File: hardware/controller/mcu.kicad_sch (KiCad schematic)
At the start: 13 parts, among them J5 Screw_Terminal_01x02, J6 Screw_Terminal_01x02, P1 USB_C_Plug_USB2.0, Q1 MMBF4392, U1 ESP32-C3-MINI-1

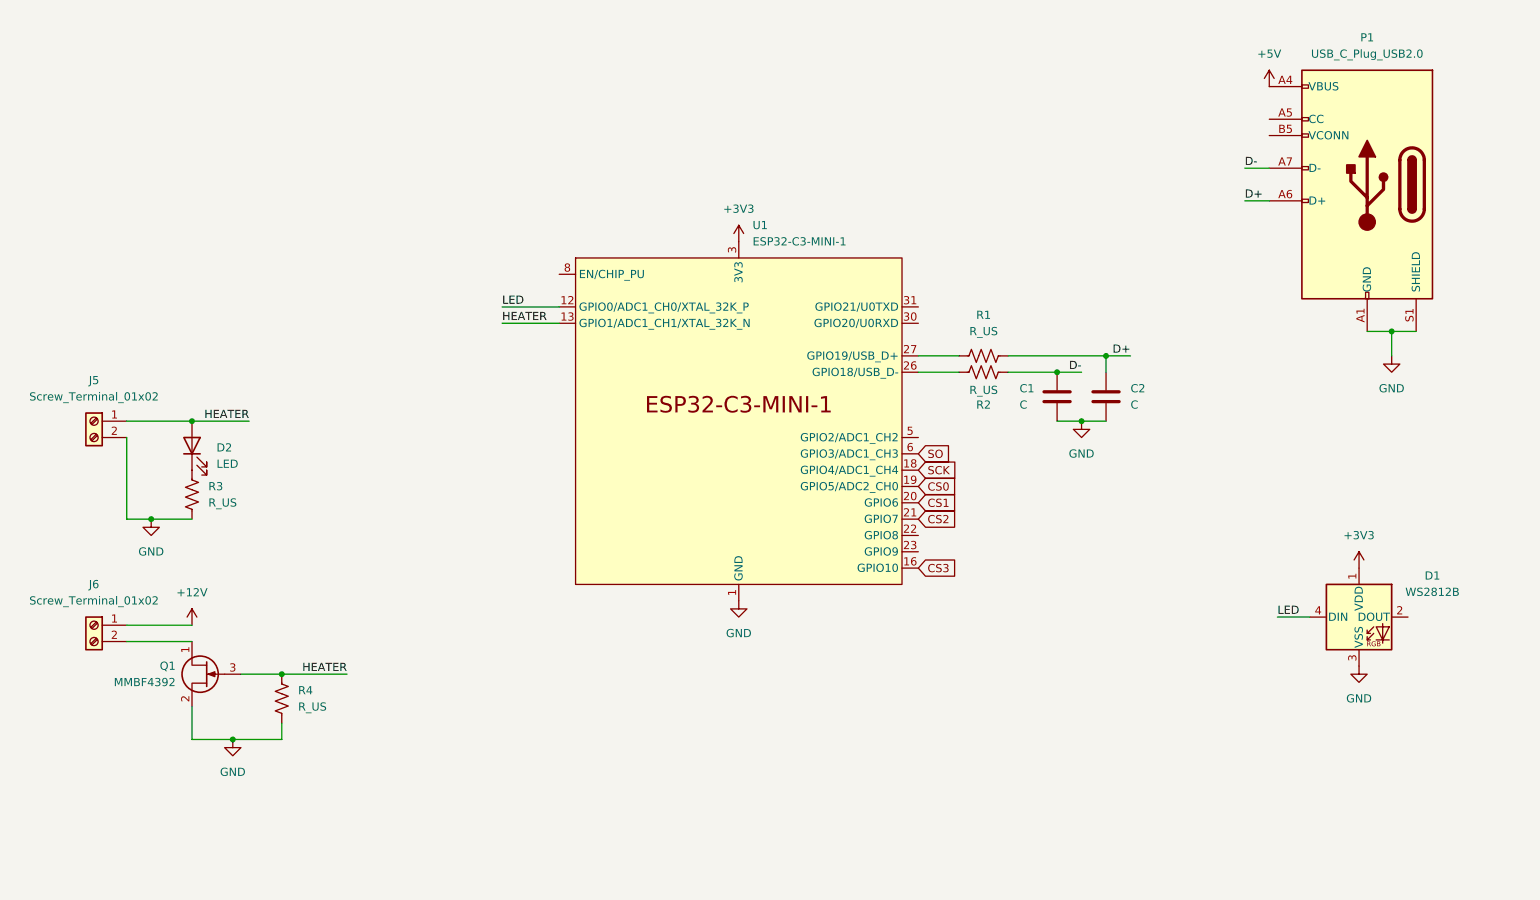
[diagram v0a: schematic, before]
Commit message: Fixed up MCU strapping pins
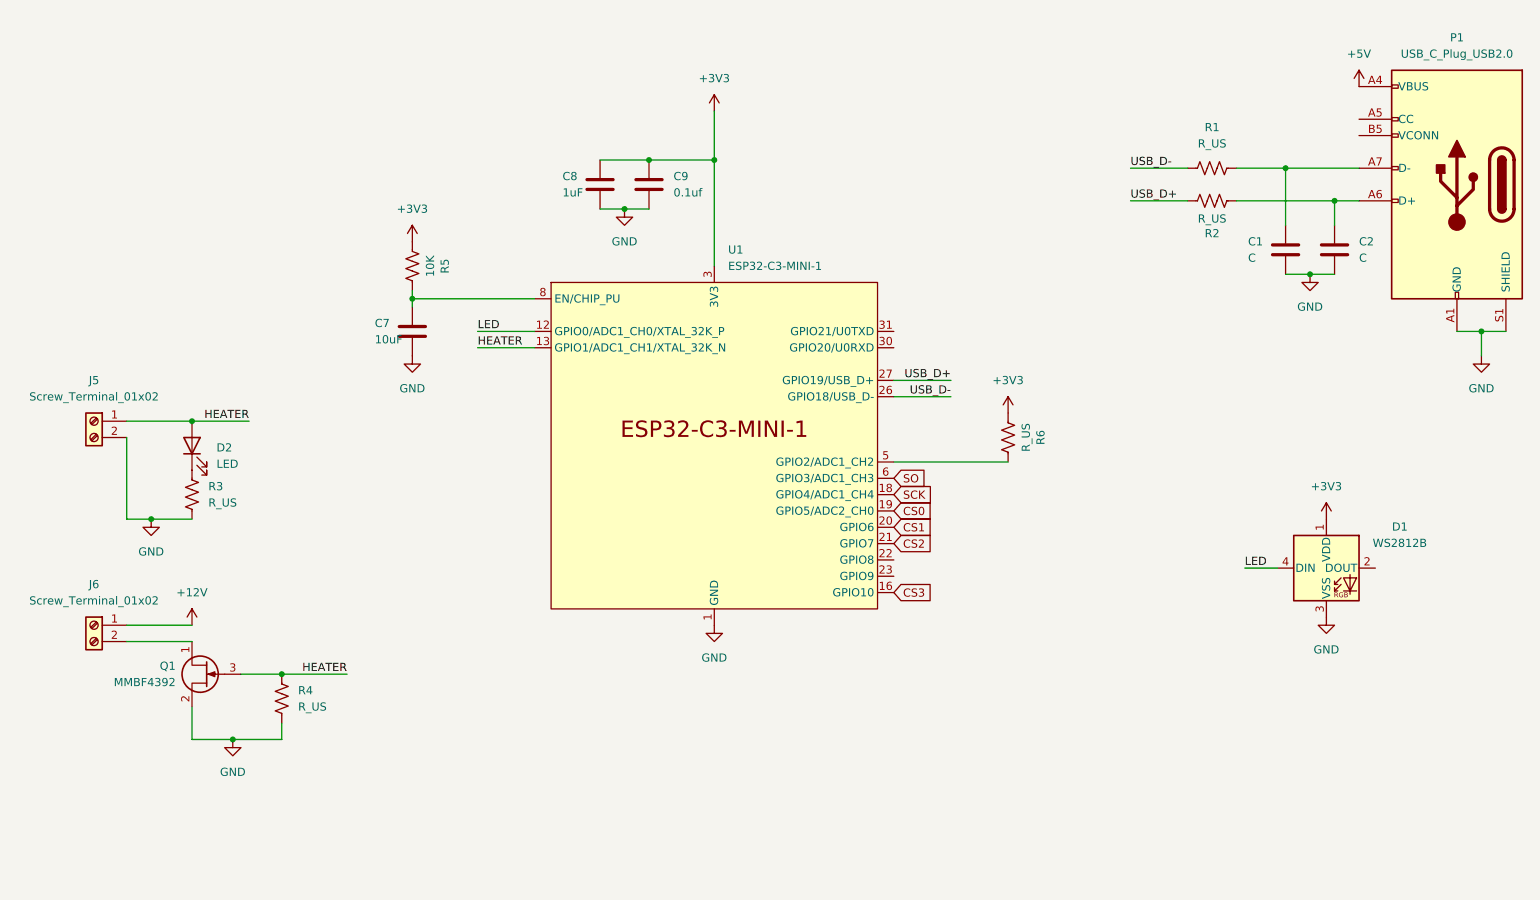
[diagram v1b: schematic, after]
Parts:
- added C7: 10uF, Capacitor_SMD:C_0805_2012Metric, symbol Device:C
- added C8: 1uF, Capacitor_SMD:C_0805_2012Metric, symbol Device:C
- added C9: 0.1uf, Capacitor_SMD:C_0805_2012Metric, symbol Device:C
- added R5: 10K, Resistor_SMD:R_0805_2012Metric, symbol Device:R_US
- added R6: R_US, Resistor_SMD:R_0805_2012Metric, symbol Device:R_US
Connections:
- net +3V3: now also C8.1, C9.1, R5.2, R6.2
- net GND: now also C7.2, C8.2, C9.2
- net USB_D+: now reaches R2.1
- net USB_D+: now also U1.27 (GPIO19/USB_D+); no longer U1.26 (GPIO18/USB_D-)
- net USB_D-: now reaches R1.1
- net USB_D-: now also U1.26 (GPIO18/USB_D-); no longer U1.27 (GPIO19/USB_D+)
- net at U1.5 (GPIO2/ADC1_CH2): now also R6.1
- net at U1.8 (EN/CHIP_PU): now also C7.1, R5.1
- net D+: no longer names the net of C2.1, P1.A6 (D+)
- net D+: now also R2.2; no longer R1.2
- net D-: no longer names the net of C1.1, P1.A7 (D-)
- net D-: now also R1.2; no longer R2.2
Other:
- moved on the sheet: C1, C2, D1, P1, R1, R2, U1

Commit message: Filled out power section of schematic
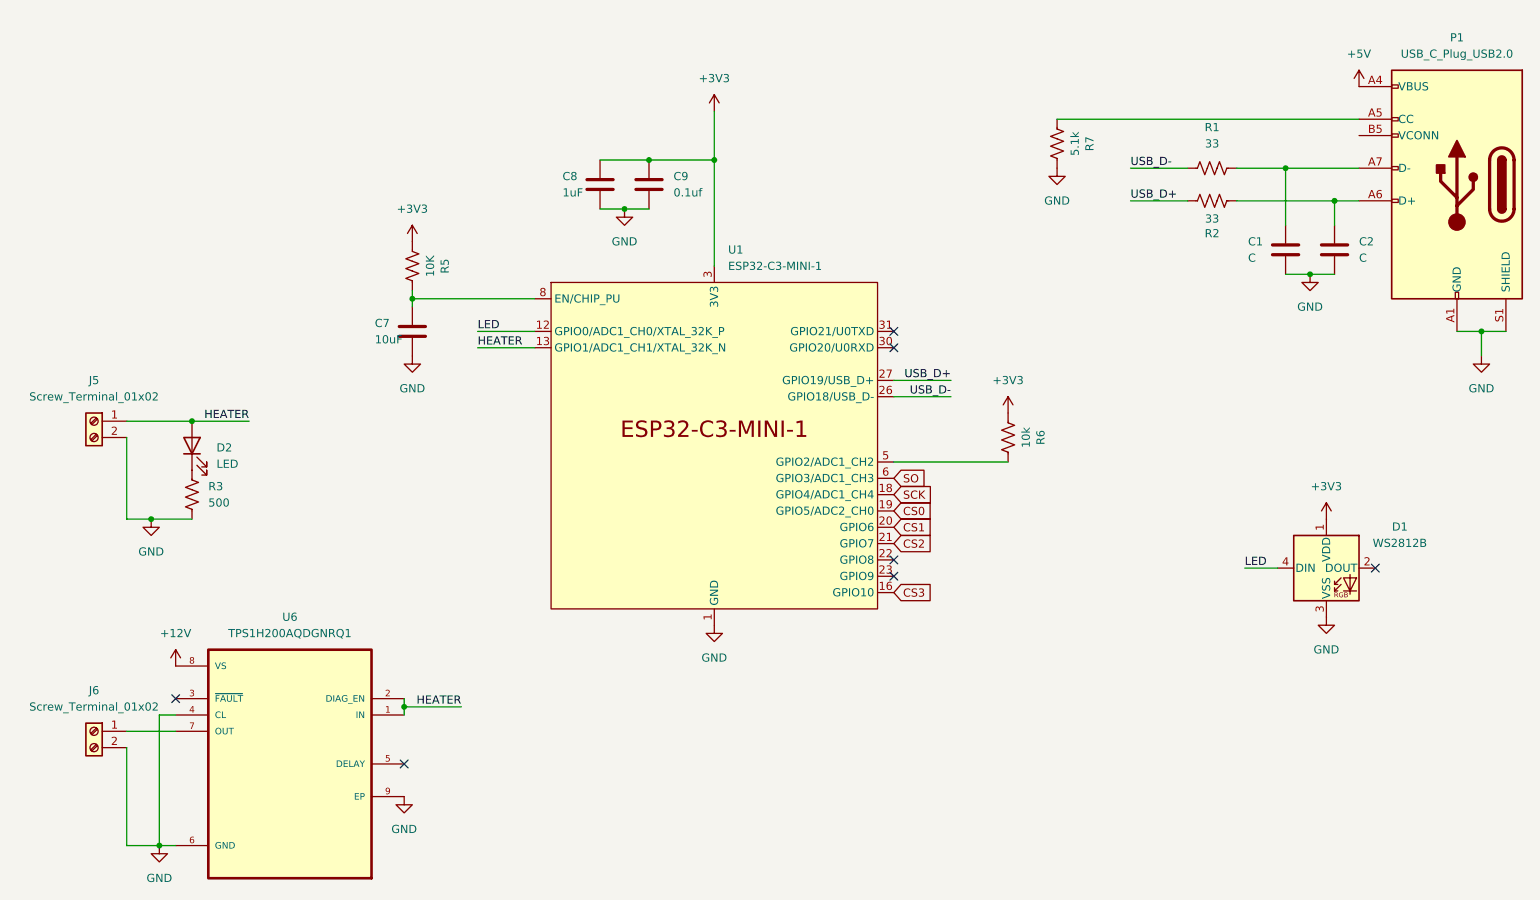
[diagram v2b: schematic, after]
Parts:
- removed Q1: MMBF4392, Package_TO_SOT_SMD:SOT-23, symbol Transistor_FET:MMBF4392
- removed R4: R_US, Resistor_SMD:R_0805_2012Metric, symbol Device:R_US
- added R7: 5.1k, Resistor_SMD:R_0805_2012Metric, symbol Device:R_US
- added U6: TPS1H200AQDGNRQ1, TPS1H200:SOP65P490X110-9N, symbol TPS1H200A:TPS1H200AQDGNRQ1
- R1, R2: value R_US -> 33
- R3: value R_US -> 500
- R6: value R_US -> 10k
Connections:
- net +12V: now also U6.8 (VS); no longer J6.1 (Pin_1)
- net GND: now also J6.2 (Pin_2), R7.1, U6.4 (CL), U6.6 (GND), U6.9 (EP)
- net HEATER: now also U6.1 (IN), U6.2 (DIAG_EN)
- net at P1.A5 (CC): now also R7.2
- new net: J6.1 (Pin_1), U6.7 (OUT)
- no-connect marks 0 -> 7
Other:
- moved on the sheet: J6

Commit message: Fix USB symbol, adjust decoupling caps
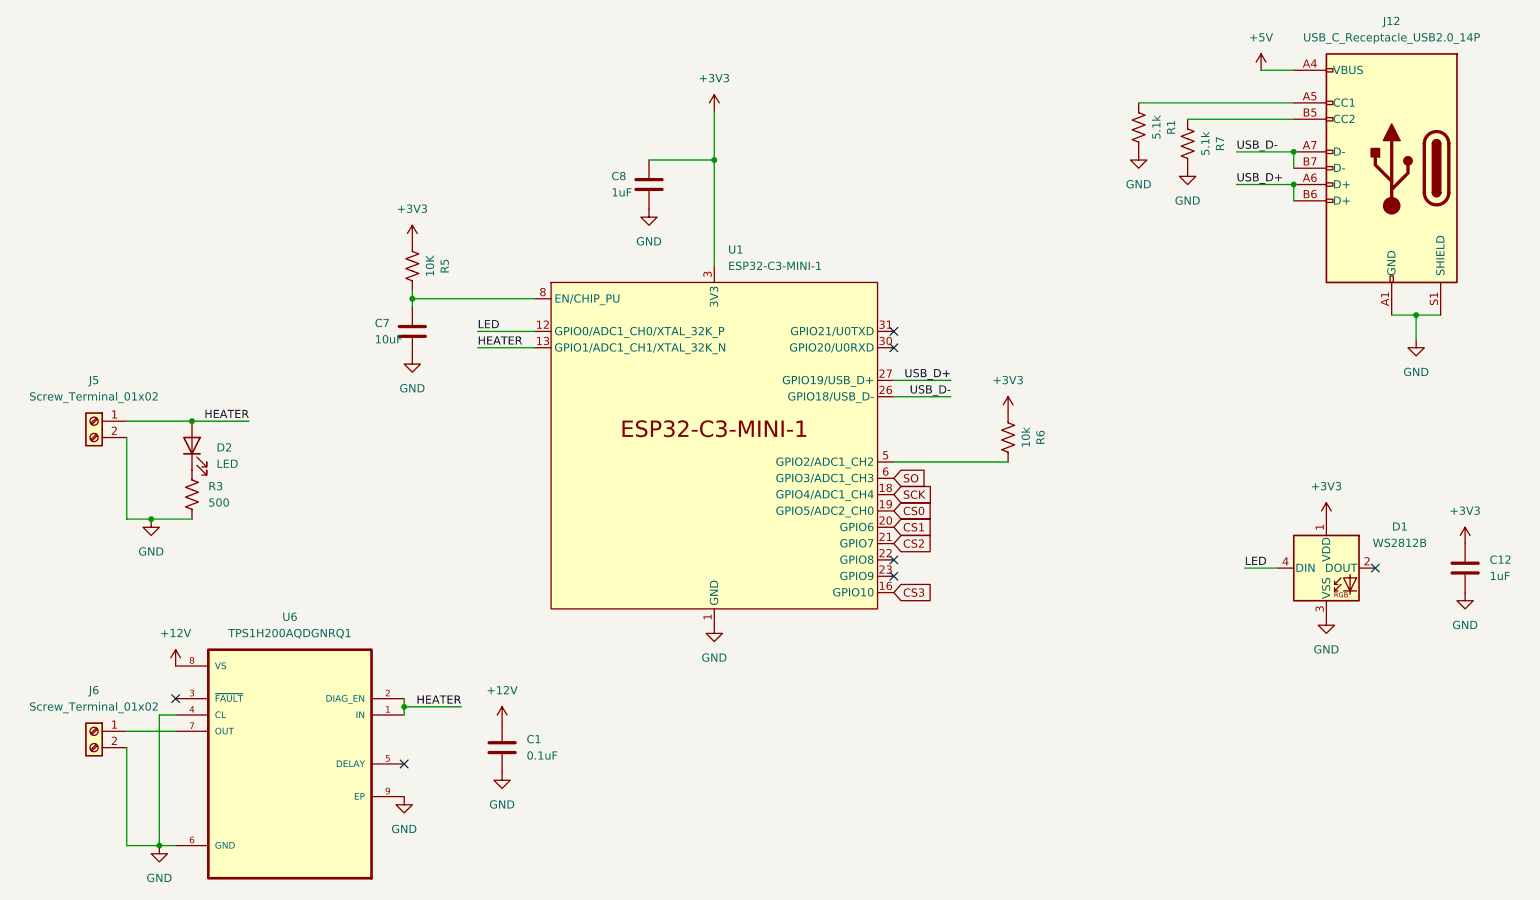
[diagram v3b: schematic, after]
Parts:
- removed C2: C, Capacitor_SMD:C_0805_2012Metric, symbol Device:C
- removed C9: 0.1uf, Capacitor_SMD:C_0805_2012Metric, symbol Device:C
- removed P1: USB_C_Plug_USB2.0, Connector_USB:USB_C_Receptacle_GCT_USB4135-GF-A_6P_TopMnt_Horizontal, symbol Connector:USB_C_Plug_USB2.0
- removed R2: 33, Resistor_SMD:R_0805_2012Metric, symbol Device:R_US
- added C12: 1uF, Capacitor_SMD:C_0805_2012Metric, symbol Device:C
- added J12: USB_C_Receptacle_USB2.0_14P, symbol Connector:USB_C_Receptacle_USB2.0_14P
- C1: value C -> 0.1uF
- R1: value 33 -> 5.1k
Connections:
- net +12V: now also C1.1
- net +3V3: now also C12.1
- net +5V: now also J12.A4 (VBUS), J12.A9 (VBUS), J12.B4 (VBUS), J12.B9 (VBUS)
- net GND: now also R1.1, C12.2, J12.A1 (GND), J12.A12 (GND), J12.B1 (GND), J12.B12 (GND), J12.S1 (SHIELD)
- net USB_D+: now also J12.A6 (D+), J12.B6 (D+)
- net USB_D-: now also J12.A7 (D-), J12.B7 (D-); no longer R1.1
- net at R7.2: now also J12.B5 (CC2)
- net at R1.2: now also J12.A5 (CC1); no longer C1.1
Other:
- moved on the sheet: C8, R7

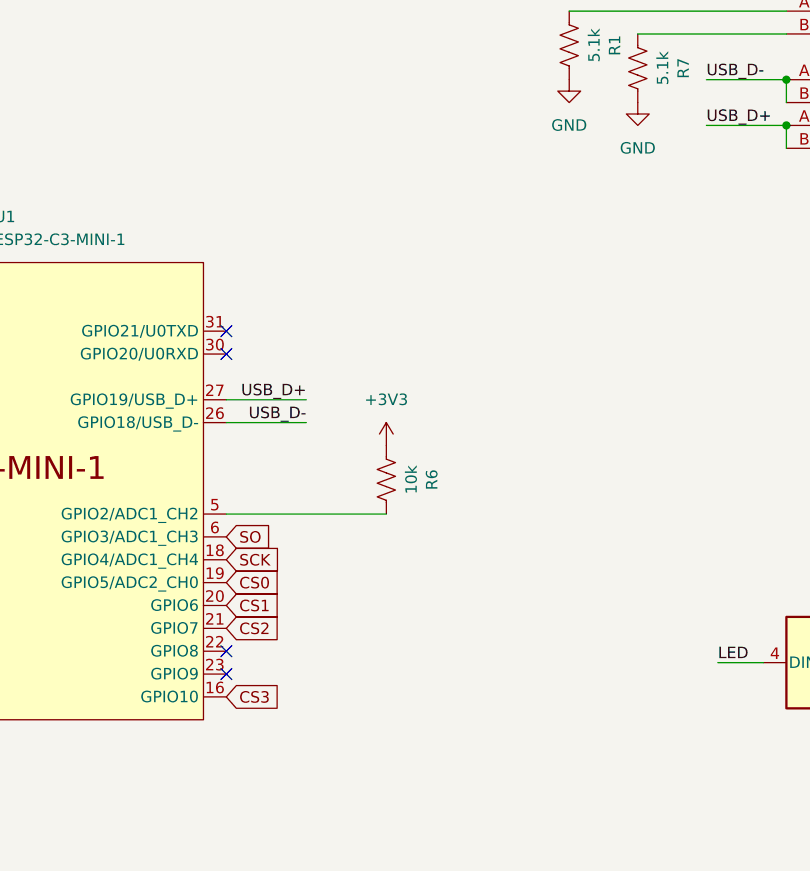
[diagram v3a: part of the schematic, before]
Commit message: Drop to 3x thermocouples, 2x fans
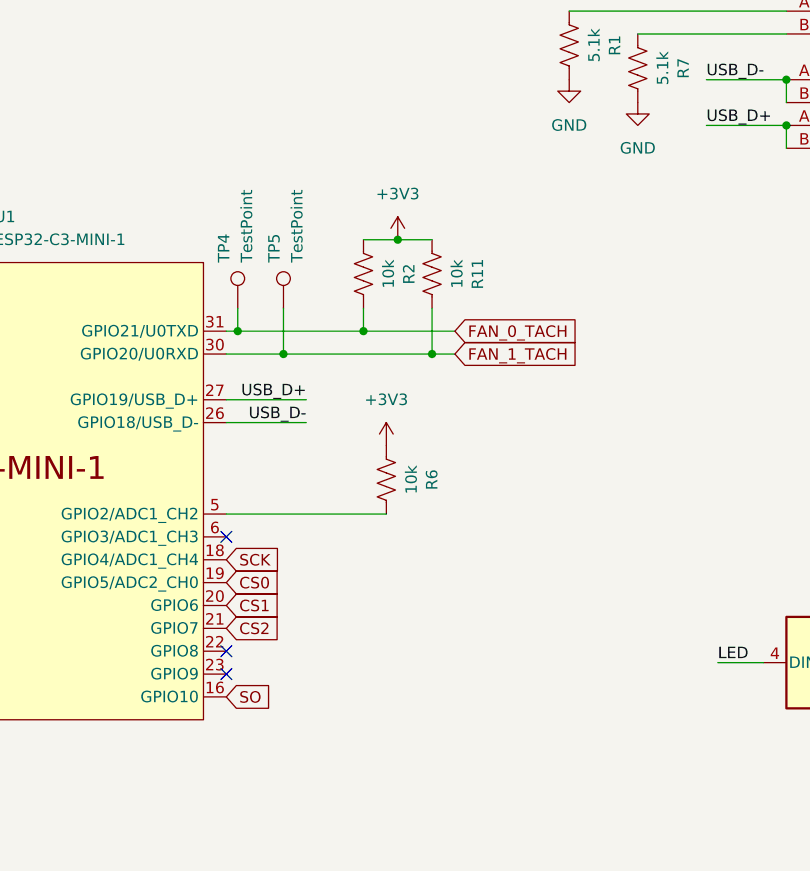
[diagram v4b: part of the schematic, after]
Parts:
- added R11, R2: 10k, Resistor_SMD:R_0805_2012Metric, symbol Device:R_US
- added TP4, TP5: TestPoint, TestPoint:TestPoint_Pad_D2.0mm, symbol Connector:TestPoint
- J12: footprint (none) -> Connector_USB:USB_C_Receptacle_GCT_USB4105-xx-A_16P_TopMnt_Horizontal
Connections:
- net CS3 is gone; now on net SO: U1.16 (GPIO10)
- net +3V3: now also R11.2, R2.2
- net SO: no longer U1.6 (GPIO3/ADC1_CH3)
- net FAN_1_TACH: now reaches U1.30 (GPIO20/U0RXD)
- net FAN_1_TACH: now also R11.1, TP5.1
- net FAN_0_TACH: now reaches U1.31 (GPIO21/U0TXD)
- net FAN_0_TACH: now also R2.1, TP4.1
- no-connect marks 7 -> 6

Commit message: First stab at board routing
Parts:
- TP4, TP5: footprint TestPoint:TestPoint_Pad_D2.0mm -> TestPoint:TestPoint_THTPad_2.0x2.0mm_Drill1.0mm
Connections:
- net CS0: now also U1.18 (GPIO4/ADC1_CH4); no longer U1.19 (GPIO5/ADC2_CH0)
- net SCK: now also U1.19 (GPIO5/ADC2_CH0); no longer U1.18 (GPIO4/ADC1_CH4)
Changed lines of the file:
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@@
 	(global_label "SCK"
 		(shape input)
-		(at 173.99 100.33 0)
+		(at 173.99 102.87 0)
 		(fields_autoplaced yes)
 		(effects
@@
 		)
 		(property "Intersheetrefs" "${INTERSHEET_REFS}"
-			(at 180.7247 100.33 0)
+			(at 180.7247 102.87 0)
 			(effects
 				(font
@@
 	(global_label "CS0"
 		(shape input)
-		(at 173.99 102.87 0)
+		(at 173.99 100.33 0)
 		(fields_autoplaced yes)
 		(effects
@@
 		)
 		(property "Intersheetrefs" "${INTERSHEET_REFS}"
-			(at 180.6642 102.87 0)
+			(at 180.6642 100.33 0)
 			(effects
 				(font
@@
 			)
 		)
-		(property "Footprint" "TestPoint:TestPoint_Pad_D2.0mm"
+		(property "Footprint" "TestPoint:TestPoint_THTPad_2.0x2.0mm_Drill1.0mm"
 			(at 180.34 72.39 0)
 			(effects
@@
 			)
 		)
-		(property "Footprint" "TestPoint:TestPoint_Pad_D2.0mm"
+		(property "Footprint" "TestPoint:TestPoint_THTPad_2.0x2.0mm_Drill1.0mm"
 			(at 185.42 72.39 0)
 			(effects

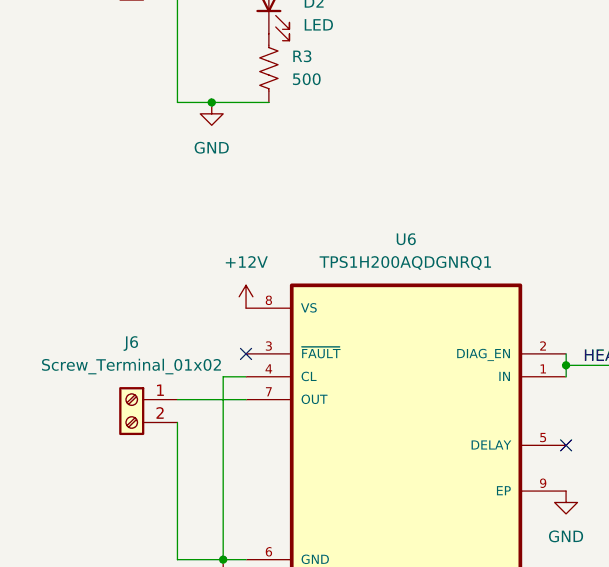
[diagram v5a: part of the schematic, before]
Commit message: Layout tweaks
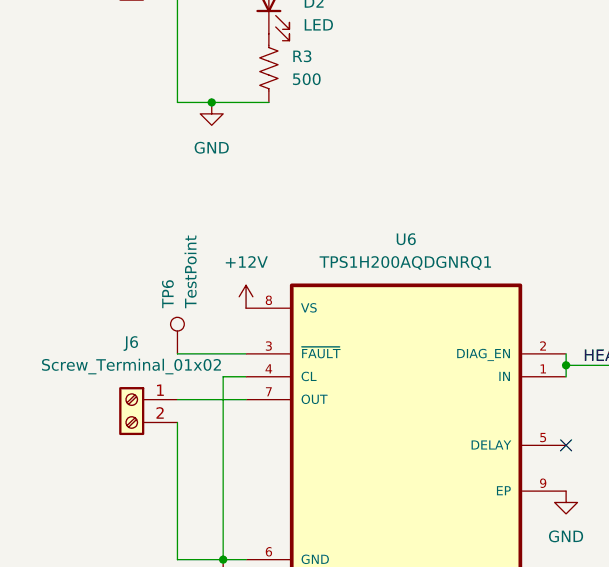
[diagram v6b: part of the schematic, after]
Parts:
- added TP6: TestPoint, TestPoint:TestPoint_THTPad_2.0x2.0mm_Drill1.0mm, symbol Connector:TestPoint
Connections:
- net at U6.3 (~{FAULT}): now also TP6.1
- no-connect marks 6 -> 5
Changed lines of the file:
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@@
 	)
 	(no_connect
-		(at 62.23 132.08)
-	)
-	(no_connect
 		(at 173.99 113.03)
 	)
@@
 	(wire
 		(pts
+			(xy 54.61 132.08) (xy 62.23 132.08)
+		)
+		(stroke
+			(width 0)
+			(type default)
+		)
+	)
+	(wire
+		(pts
 			(xy 175.26 74.93) (xy 189.23 74.93)
 		)
@@
 					(unit 1)
 				)
+			)
+		)
+	)
+	(symbol
+		(lib_id "Connector:TestPoint")
+		(at 54.61 132.08 0)
+		(unit 1)
+		(exclude_from_sim no)
+		(in_bom yes)
+		(on_board yes)
+		(dnp no)
+		(property "Reference" "TP6"
+			(at 53.594 127 90)
+			(effects
+				(font
+					(size 1.27 1.27)
+				)
+				(justify left)
+			)
+		)
+		(property "Value" "TestPoint"
+			(at 56.134 127 90)
+			(effects
+				(font
+					(size 1.27 1.27)
+				)
+				(justify left)
+			)
+		)
+		(property "Footprint" "TestPoint:TestPoint_THTPad_2.0x2.0mm_Drill1.0mm"
+			(at 59.69 132.08 0)
+			(effects
+				(font
+					(size 1.27 1.27)
+				)
+				(hide yes)
+			)
+		)
+		(property "Datasheet" "~"
+			(at 59.69 132.08 0)
+			(effects
+				(font
+					(size 1.27 1.27)
+				)
+				(hide yes)
+			)
+		)
+		(property "Description" "test point"
+			(at 54.61 132.08 0)
+			(effects
+				(font
+					(size 1.27 1.27)
+				)
+				(hide yes)
+			)
+		)
+		(pin "1"
+		)
+		(instances
+			(project "controller"
+				(path "/3ee12552-bbaf-4643-8241-99077a41063f/0cb4d016-03f6-42de-b902-af7c075bf798"
+					(reference "TP6")
+					(unit 1)
+				)
